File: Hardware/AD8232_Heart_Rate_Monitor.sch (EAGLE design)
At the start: 40 parts, among them U1 AD8232

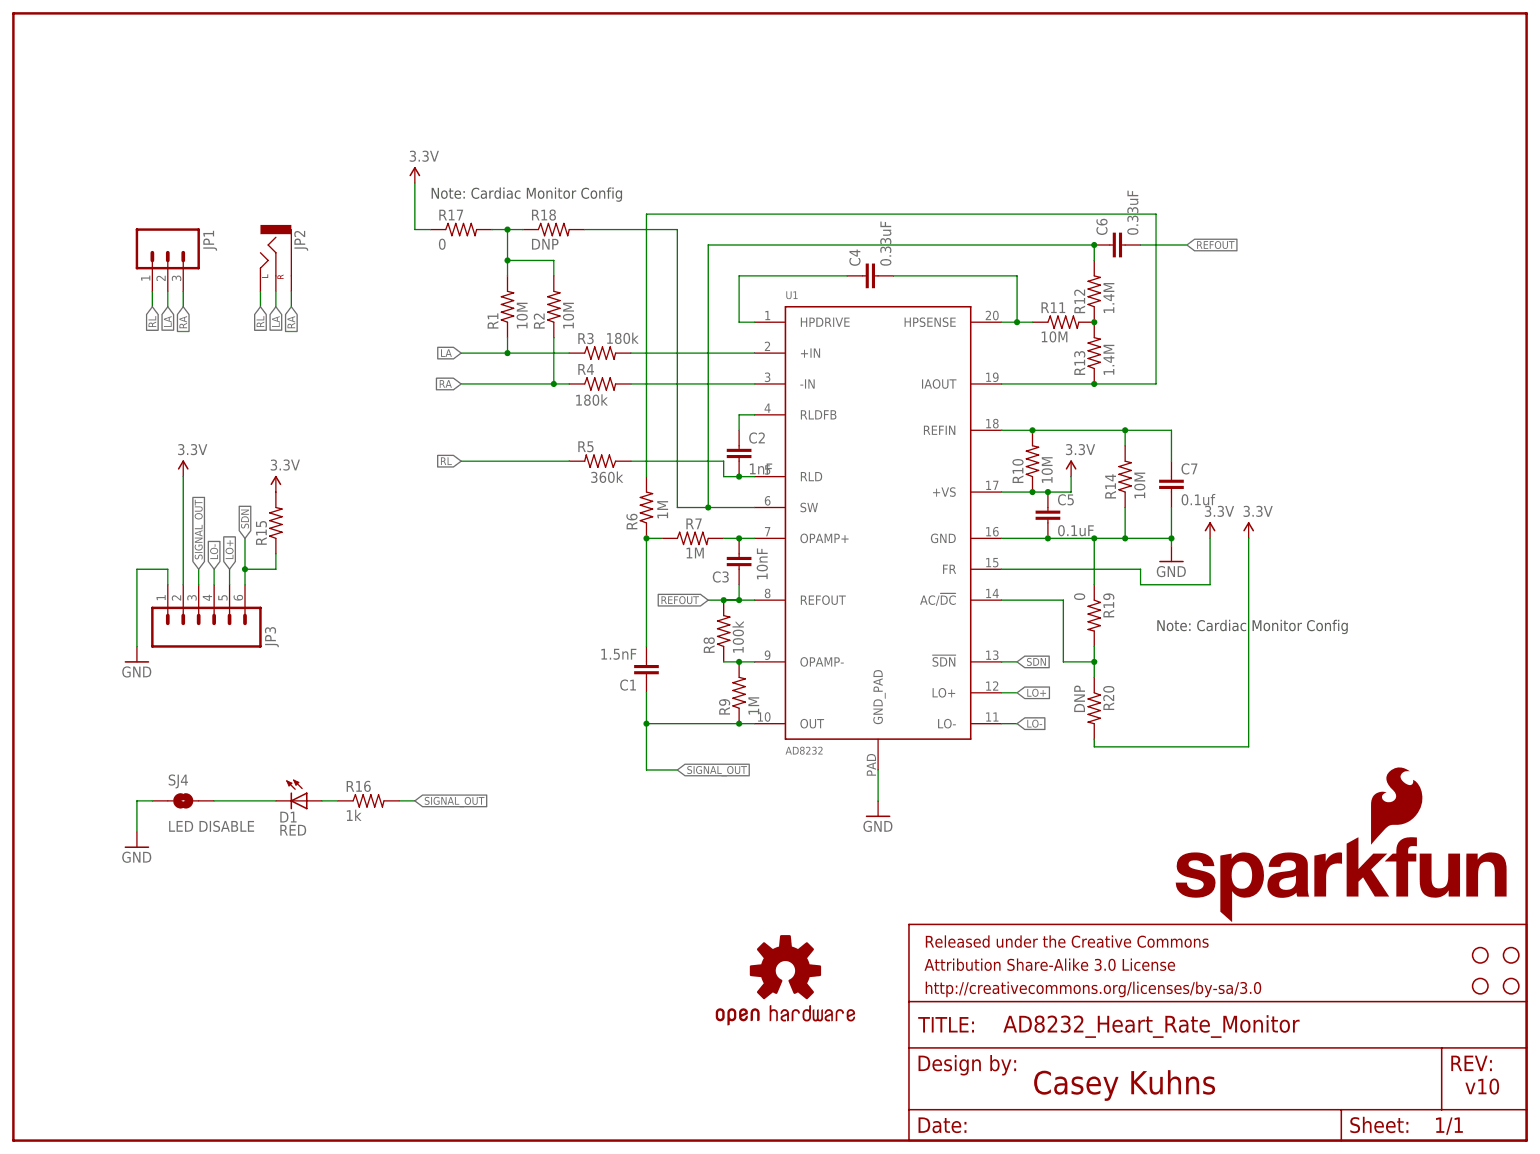
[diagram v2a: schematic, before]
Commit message: Changed layout in attempt to remove noise.  Changed resistor values to help remove DC offset.
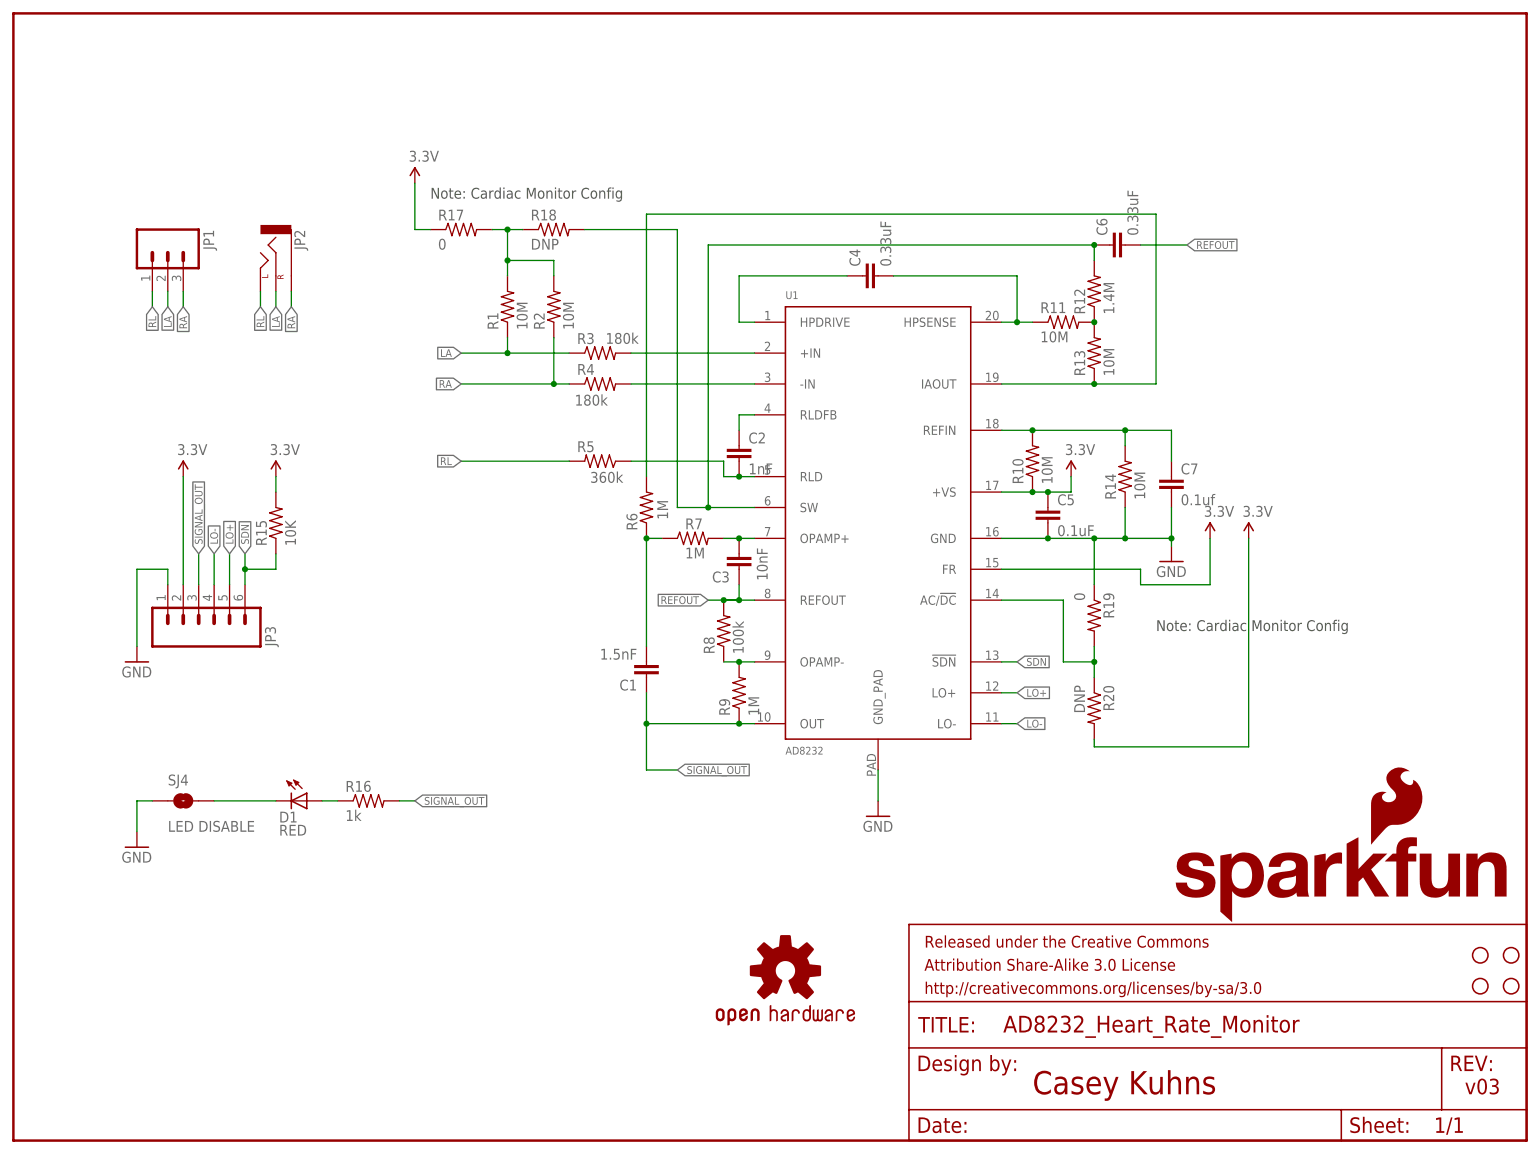
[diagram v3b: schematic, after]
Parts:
- R13: value 1.4M -> 10M
- R15: value (none) -> 10K
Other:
- note added: "v03"
- note removed: "v10"
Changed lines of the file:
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@@
 <part name="R1" library="SparkFun-Passives" deviceset="RESISTOR" device="0603-RES" value="10M"/>
 <part name="R12" library="SparkFun-Passives" deviceset="RESISTOR" device="0603-RES" value="1.4M"/>
-<part name="R13" library="SparkFun-Passives" deviceset="RESISTOR" device="0603-RES" value="1.4M"/>
+<part name="R13" library="SparkFun-Passives" deviceset="RESISTOR" device="0603-RES" value="10M"/>
 <part name="R14" library="SparkFun-Passives" deviceset="RESISTOR" device="0603-RES" value="10M"/>
 <part name="R6" library="SparkFun-Passives" deviceset="RESISTOR" device="0603-RES" value="1M"/>
@@
 <part name="LOGO1" library="SparkFun-Aesthetics" deviceset="OSHW-LOGO" device="S"/>
 <part name="JP3" library="SparkFun-Connectors" deviceset="M06" device="SIP"/>
-<part name="R15" library="SparkFun-Resistors" deviceset="10KOHM1/10W1%(0603)" device="0603"/>
+<part name="R15" library="SparkFun-Resistors" deviceset="10KOHM1/10W1%(0603)" device="0603" value="10K"/>
 <part name="SUPPLY6" library="SparkFun-Aesthetics" deviceset="3.3V" device=""/>
 <part name="JP1" library="SparkFun-Connectors" deviceset="M03" device="PTH"/>
@@
 <plain>
 <text x="167.64" y="7.62" size="3.81" layer="94" font="vector">Casey Kuhns</text>
-<text x="238.76" y="7.62" size="2.54" layer="94" font="vector">v10</text>
+<text x="238.76" y="7.62" size="2.54" layer="94" font="vector">v03</text>
 <text x="68.58" y="154.94" size="1.778" layer="97">Note: Cardiac Monitor Config</text>
 <text x="187.96" y="83.82" size="1.778" layer="97">Note: Cardiac Monitor Config</text>
@@
 <instance part="JP3" gate="G$1" x="30.48" y="86.36" rot="MR90"/>
 <instance part="R15" gate="G$1" x="43.18" y="101.6" rot="R90"/>
-<instance part="SUPPLY6" gate="G$1" x="43.18" y="106.68"/>
+<instance part="SUPPLY6" gate="G$1" x="43.18" y="109.22"/>
 <instance part="JP1" gate="G$1" x="25.4" y="147.32" rot="R270"/>
 <instance part="R16" gate="G$1" x="58.42" y="55.88"/>
@@
 <segment>
 <pinref part="JP3" gate="G$1" pin="3"/>
-<wire x1="30.48" y1="91.44" x2="30.48" y2="93.98" width="0.1524" layer="91"/>
-<label x="30.48" y="93.98" size="1.27" layer="95" rot="R90" xref="yes"/>
+<wire x1="30.48" y1="91.44" x2="30.48" y2="96.52" width="0.1524" layer="91"/>
+<label x="30.48" y="96.52" size="1.27" layer="95" rot="R90" xref="yes"/>
 </segment>
 <segment>
@@
 <pinref part="R15" gate="G$1" pin="2"/>
 <pinref part="SUPPLY6" gate="G$1" pin="3.3V"/>
+<wire x1="43.18" y1="109.22" x2="43.18" y2="106.68" width="0.1524" layer="91"/>
 </segment>
 </net>
@@
 </segment>
 <segment>
-<wire x1="35.56" y1="91.44" x2="35.56" y2="93.98" width="0.1524" layer="91"/>
-<label x="35.56" y="93.98" size="1.27" layer="95" rot="R90" xref="yes"/>
+<wire x1="35.56" y1="91.44" x2="35.56" y2="96.52" width="0.1524" layer="91"/>
+<label x="35.56" y="96.52" size="1.27" layer="95" rot="R90" xref="yes"/>
 <pinref part="JP3" gate="G$1" pin="5"/>
 </segment>
@@
 </segment>
 <segment>
-<wire x1="33.02" y1="91.44" x2="33.02" y2="93.98" width="0.1524" layer="91"/>
-<label x="33.02" y="93.98" size="1.27" layer="95" rot="R90" xref="yes"/>
+<wire x1="33.02" y1="91.44" x2="33.02" y2="96.52" width="0.1524" layer="91"/>
+<label x="33.02" y="96.52" size="1.27" layer="95" rot="R90" xref="yes"/>
 <pinref part="JP3" gate="G$1" pin="4"/>
 </segment>
@@
 <segment>
 <wire x1="38.1" y1="91.44" x2="38.1" y2="93.98" width="0.1524" layer="91"/>
-<label x="38.1" y="99.06" size="1.27" layer="95" rot="R90" xref="yes"/>
+<label x="38.1" y="96.52" size="1.27" layer="95" rot="R90" xref="yes"/>
 <pinref part="JP3" gate="G$1" pin="6"/>
-<wire x1="38.1" y1="93.98" x2="38.1" y2="99.06" width="0.1524" layer="91"/>
+<wire x1="38.1" y1="93.98" x2="38.1" y2="96.52" width="0.1524" layer="91"/>
 <wire x1="38.1" y1="93.98" x2="43.18" y2="93.98" width="0.1524" layer="91"/>
 <wire x1="43.18" y1="93.98" x2="43.18" y2="96.52" width="0.1524" layer="91"/>

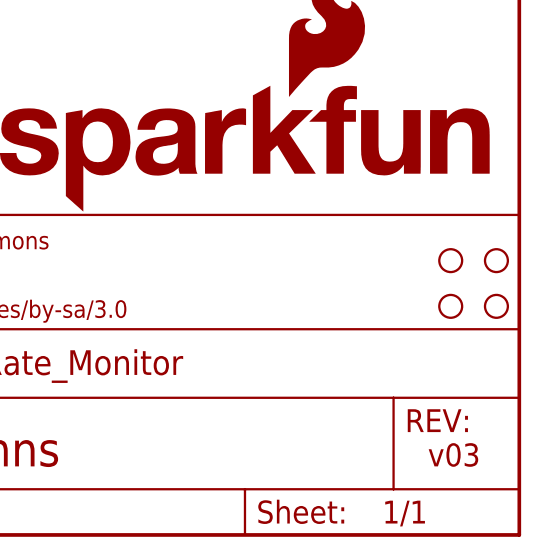
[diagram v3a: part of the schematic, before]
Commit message: Added fiducials
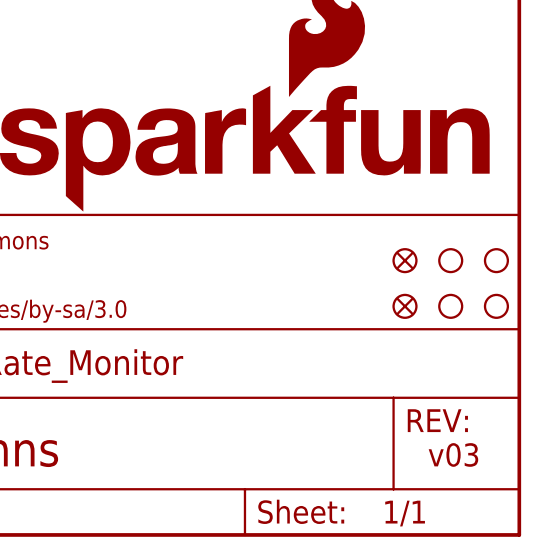
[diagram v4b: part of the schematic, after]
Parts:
- added FID1, FID2: FIDUCIAL1X2, SparkFun-Aesthetics:FIDUCIAL1X2
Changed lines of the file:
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@@
 <part name="R19" library="SparkFun-Resistors" deviceset="0OHM1/10W5%(0603)" device="" value="0"/>
 <part name="R20" library="SparkFun-Resistors" deviceset="0OHM1/10W5%(0603)" device="" value="DNP"/>
+<part name="FID1" library="SparkFun-Aesthetics" deviceset="FIDUCIAL" device="1X2"/>
+<part name="FID2" library="SparkFun-Aesthetics" deviceset="FIDUCIAL" device="1X2"/>
 </parts>
 <sheets>
@@
 <instance part="R19" gate="G$1" x="177.8" y="86.36" rot="R270"/>
 <instance part="R20" gate="G$1" x="177.8" y="71.12" rot="R270"/>
+<instance part="FID1" gate="G$1" x="236.22" y="30.48"/>
+<instance part="FID2" gate="G$1" x="236.22" y="25.4"/>
 </instances>
 <busses>

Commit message: fixed Rev Numbers
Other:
- note added: "v10"
- note removed: "v03"
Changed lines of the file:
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@@
 <plain>
 <text x="167.64" y="7.62" size="3.81" layer="94" font="vector">Casey Kuhns</text>
-<text x="238.76" y="7.62" size="2.54" layer="94" font="vector">v03</text>
+<text x="238.76" y="7.62" size="2.54" layer="94" font="vector">v10</text>
 <text x="68.58" y="154.94" size="1.778" layer="97">Note: Cardiac Monitor Config</text>
 <text x="187.96" y="83.82" size="1.778" layer="97">Note: Cardiac Monitor Config</text>
